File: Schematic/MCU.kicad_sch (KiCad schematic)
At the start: 23 parts, among them IC3 STM32H743VIT6, J1 USB_C_Receptacle_USB2.0_16P, SW1 TS24CA, Y1 Crystal

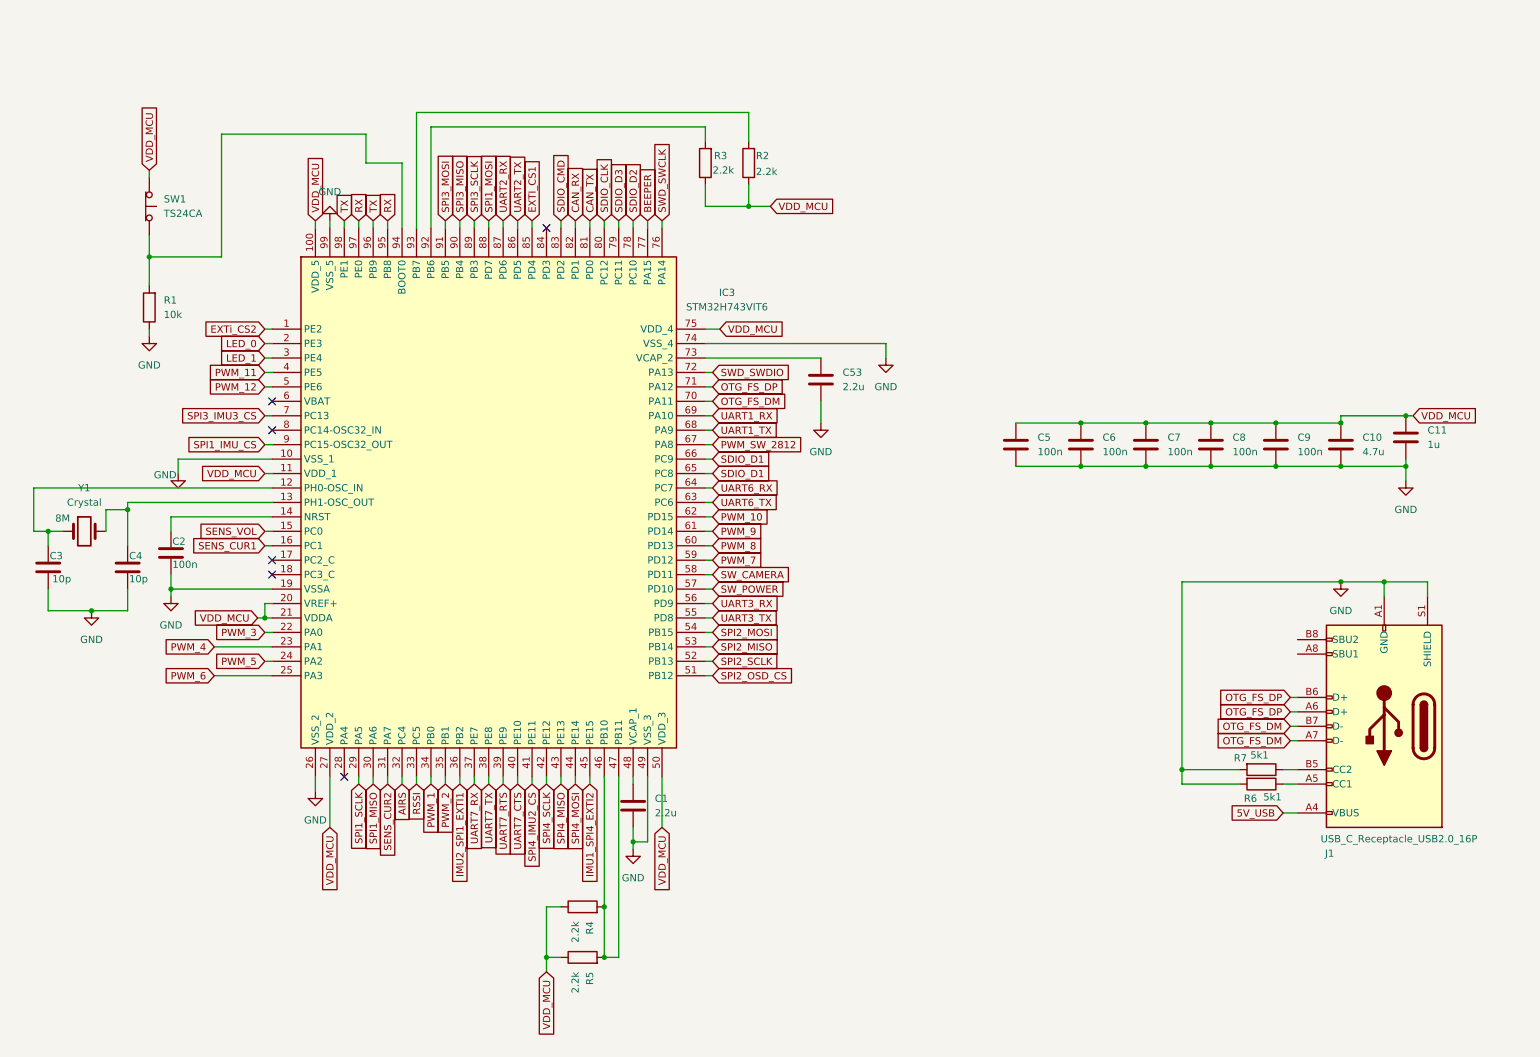
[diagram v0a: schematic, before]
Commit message: schematic fully finished, every footprint assigned, still electrical checking to do
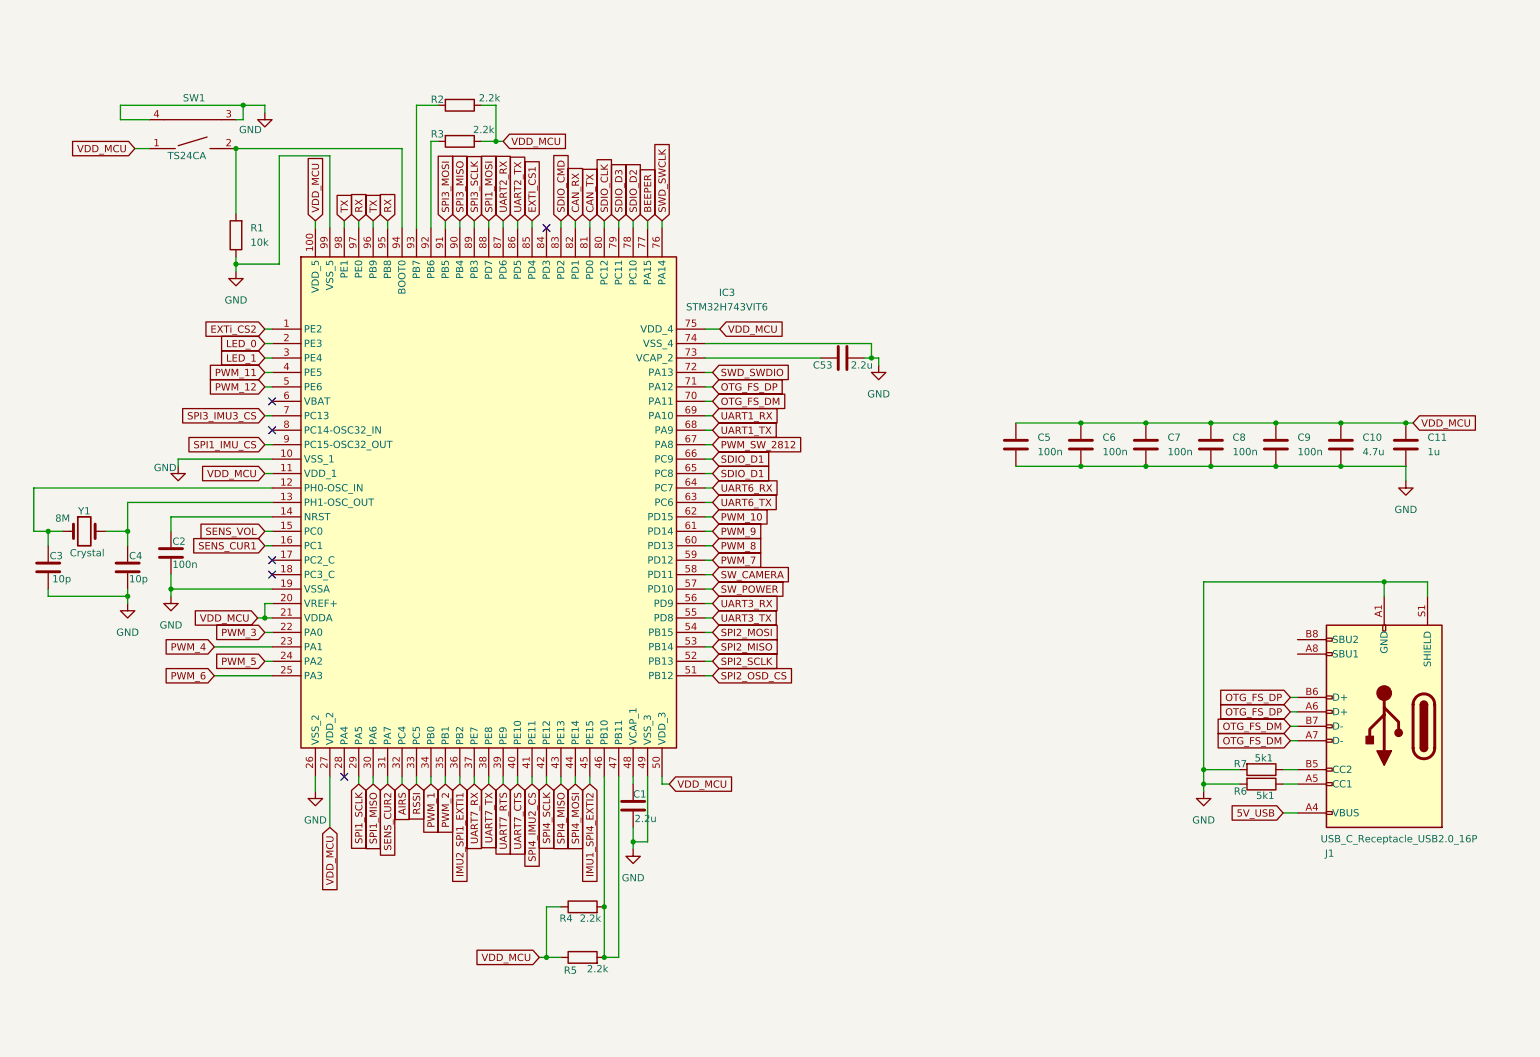
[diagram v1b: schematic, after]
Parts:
- removed SW1: TS24CA, symbol Switch:SW_Push_Open
- added SW1: TS24CA, ProLib_pcs_2025-11-24:SW-SMD_2P-TS24CA, symbol fch7_sym:TS24CA
- IC3: footprint QFP50P1600X1600X160-100M -> fch7_fp:QFP50P1600X1600X160-100M
- J1: MPN (none) -> USB4105-GF-A; ref USB4105-GF-A -> (none)
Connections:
- net GND: now also SW1.3, SW1.4
- net VDD_MCU: now also SW1.1
- net at IC3.94 (BOOT0), R1.2: now also SW1.2
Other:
- moved on the sheet: C11, C53, R1, R2, R3

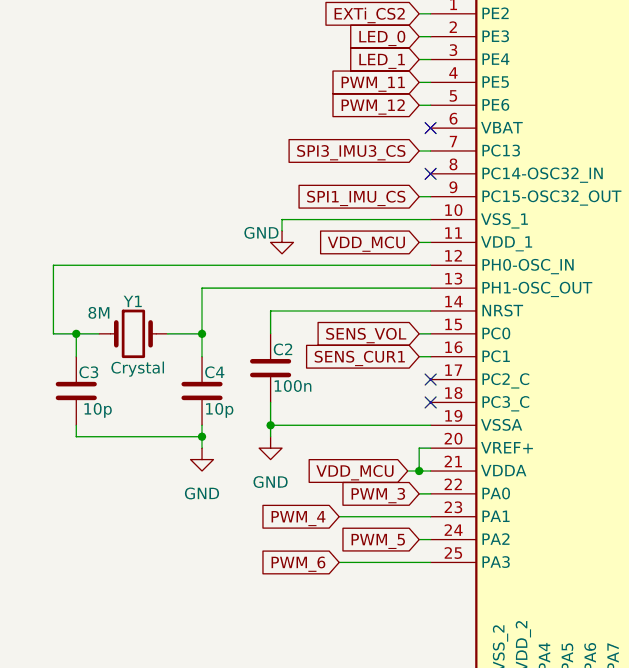
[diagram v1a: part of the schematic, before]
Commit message: reviewing and refactoring footprints and full schematic
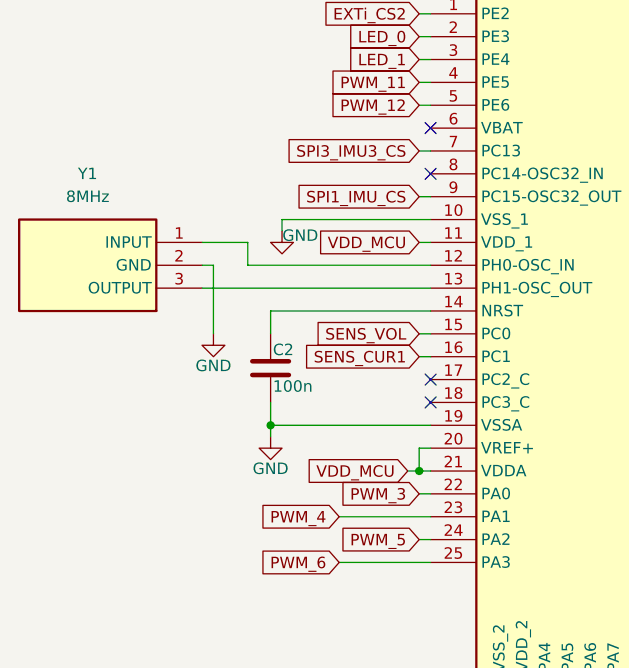
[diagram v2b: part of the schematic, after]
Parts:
- removed C3, C4: 10p, Capacitor_SMD:C_0603_1608Metric, symbol Device:C
- removed Y1: Crystal, Crystal:Crystal_SMD_3225-4Pin_3.2x2.5mm, symbol Device:Crystal
- added Y1: 8MHz, fch7_fp:CSTNE8M00G55Z000R0, symbol CSTNE8M00G55Z000R0:CSTNE8M00G55Z000R0
- C1, C53: footprint Capacitor_SMD:C_0805_2012Metric -> Capacitor_SMD:C_0603_1608Metric; MPN (none) -> CL10A225KB8NNNC; Manufacturer (none) -> SAMSUNG; Price (none) -> 0.095
- C10: footprint Capacitor_SMD:C_0805_2012Metric -> Capacitor_SMD:C_0603_1608Metric; MPN (none) -> CL10B105KO8NNNC; Manufacturer (none) -> SAMSUNG
- C11: MPN (none) -> CL10A105KB8NNNC; Manufacturer (none) -> SAMSUNG
- C2, C5, C6, C7, C8, C9: MPN (none) -> 0603B104K500NT; Manufacturer (none) -> FH
- IC3: MPN (none) -> STM32H743VIT6; Manufacturer (none) -> STM
- J1: footprint Connector_USB:USB_C_Receptacle_GCT_USB4105-xx-A_16P_TopMnt_Horizontal -> fch7_fp:USB-C-SMD_TYPE-C-6PIN-2MD-073; MPN USB4105-GF-A -> TYPE-C 16PIN 2MD(073); Manufacturer (none) -> SHOU HAN
- R1: MPN (none) -> 0603WAF1002T5E; Manufacturer (none) -> UNI-ROYAL
- R2, R3, R4, R5: MPN (none) -> 0603WAF2201T5E; Manufacturer (none) -> UNI-ROYAL
- R6, R7: MPN (none) -> 0603WAF5101T5E; Manufacturer (none) -> UNI-ROYAL
- SW1: MPN (none) -> TS24CA
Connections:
- net GND: now also Y1.2 (GND)
- net at IC3.12 (PH0-OSC_IN): now also Y1.1 (INPUT)
- net at IC3.13 (PH1-OSC_OUT): now also Y1.3 (OUTPUT)

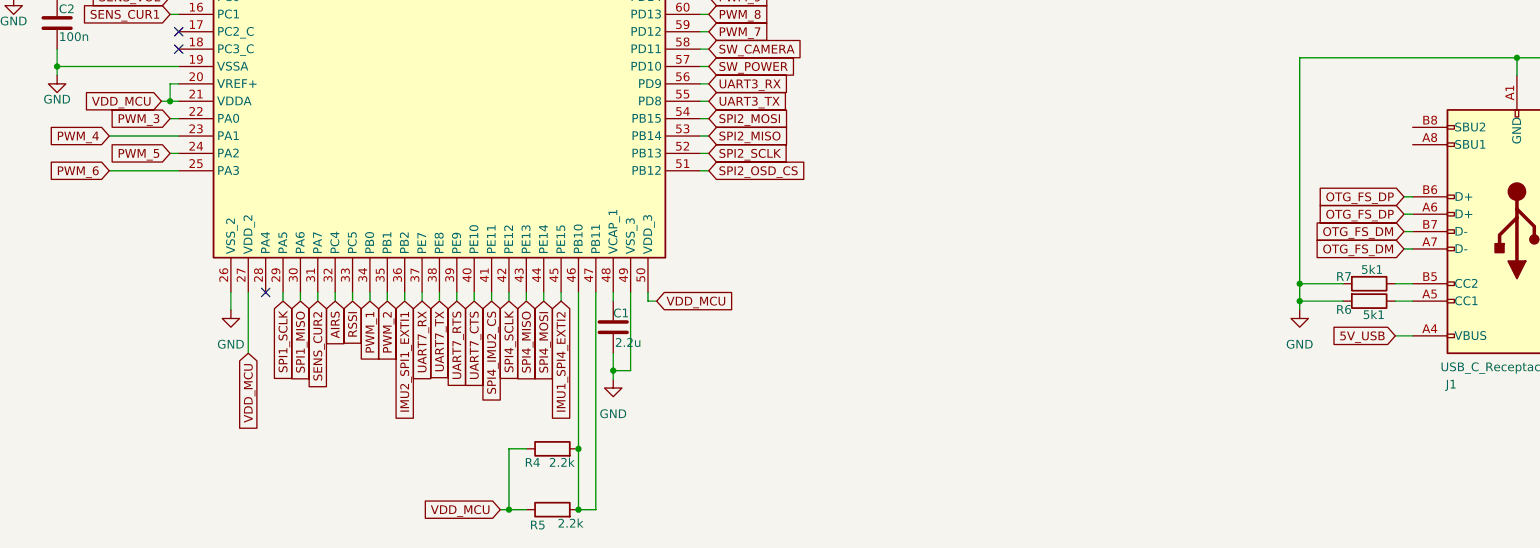
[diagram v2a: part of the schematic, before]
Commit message: Update schematic and footprint libraries with various component modifications
- Updated fp-info-cache with new component details and footprint changes.
- Modified osd.kicad_sch to correct pin types and add no_connect entries.
- Adjusted rf_rx.kicad_sch to fix pin assignments and update component properties.
- Enhanced sensors.kicad_sch with new properties for QMC5883L and SPL06-001 sensors.
- Added new libraries to sym-lib-table and fp-lib-table for better organization and access to components.
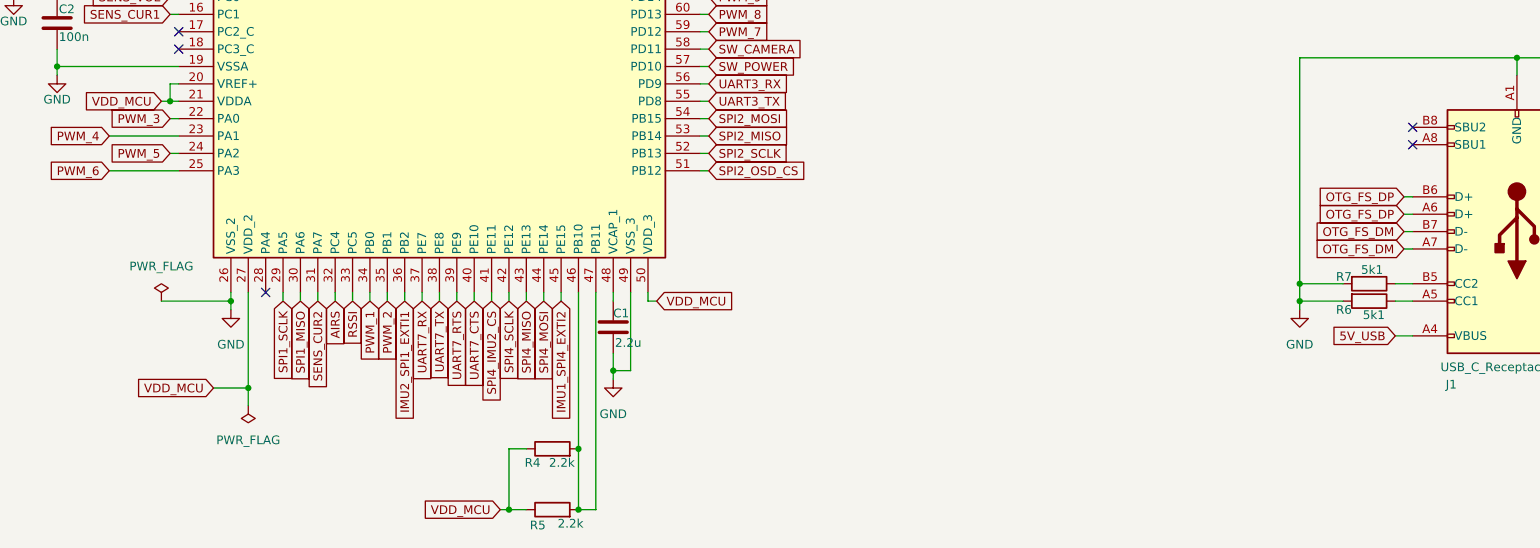
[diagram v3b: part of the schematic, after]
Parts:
- IC3: footprint fch7_fp:QFP50P1600X1600X160-100M -> fch7_fp:LQFP-100_14x14mm_P0.5mm_STM32H743
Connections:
- no-connect marks 6 -> 8
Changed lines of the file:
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@@
 	(paper "A4")
 	(junction
+		(at 71.12 148.59)
+		(diameter 0)
+		(color 0 0 0 0)
+	)
+	(junction
 		(at 205.74 85.09)
 		(diameter 0)
@@
 	)
 	(junction
+		(at 73.66 161.29)
+		(diameter 0)
+		(color 0 0 0 0)
+	)
+	(junction
 		(at 121.92 179.07)
 		(diameter 0)
@@
 	)
 	(no_connect
+		(at 243.84 123.19)
+	)
+	(no_connect
 		(at 63.5 111.76)
 	)
 	(no_connect
+		(at 243.84 125.73)
+	)
+	(no_connect
 		(at 76.2 147.32)
 	)
@@
 	(wire
 		(pts
-			(xy 73.66 147.32) (xy 73.66 156.21)
-		)
-		(stroke
-			(width 0)
-			(type default)
-		)
-	)
-	(wire
-		(pts
 			(xy 46.99 91.44) (xy 63.5 91.44)
 		)
@@
 	(wire
 		(pts
+			(xy 71.12 148.59) (xy 71.12 149.86)
+		)
+		(stroke
+			(width 0)
+			(type default)
+		)
+	)
+	(wire
+		(pts
 			(xy 58.42 31.75) (xy 58.42 29.21)
 		)
@@
 	(wire
 		(pts
+			(xy 73.66 161.29) (xy 73.66 163.83)
+		)
+		(stroke
+			(width 0)
+			(type default)
+		)
+	)
+	(wire
+		(pts
 			(xy 64.77 57.15) (xy 57.15 57.15)
 		)
@@
 	(wire
 		(pts
+			(xy 60.96 148.59) (xy 71.12 148.59)
+		)
+		(stroke
+			(width 0)
+			(type default)
+		)
+	)
+	(wire
+		(pts
 			(xy 241.3 153.67) (xy 243.84 153.67)
 		)
@@
 	(wire
 		(pts
+			(xy 68.58 161.29) (xy 73.66 161.29)
+		)
+		(stroke
+			(width 0)
+			(type default)
+		)
+	)
+	(wire
+		(pts
 			(xy 91.44 147.32) (xy 91.44 148.59)
 		)
@@
 	(wire
 		(pts
-			(xy 71.12 147.32) (xy 71.12 149.86)
-		)
-		(stroke
-			(width 0)
-			(type default)
-		)
-	)
-	(wire
-		(pts
 			(xy 57.15 55.88) (xy 57.15 57.15)
 		)
@@
 	(wire
 		(pts
+			(xy 73.66 147.32) (xy 73.66 161.29)
+		)
+		(stroke
+			(width 0)
+			(type default)
+		)
+	)
+	(wire
+		(pts
 			(xy 139.7 91.44) (xy 140.97 91.44)
 		)
@@
 	(wire
 		(pts
+			(xy 71.12 147.32) (xy 71.12 148.59)
+		)
+		(stroke
+			(width 0)
+			(type default)
+		)
+	)
+	(wire
+		(pts
 			(xy 132.08 148.59) (xy 133.35 148.59)
 		)
@@
 	(global_label "VDD_MCU"
 		(shape input)
-		(at 73.66 156.21 270)
+		(at 68.58 161.29 180)
 		(fields_autoplaced yes)
 		(effects
@@
 		)
 		(property "Intersheetrefs" "${INTERSHEET_REFS}"
-			(at 73.66 167.8433 90)
+			(at 56.9467 161.29 0)
 			(effects
 				(font
@@
 	)
 	(symbol
+		(lib_id "power:PWR_FLAG")
+		(at 73.66 163.83 180)
+		(unit 1)
+		(exclude_from_sim no)
+		(in_bom yes)
+		(on_board yes)
+		(dnp no)
+		(fields_autoplaced yes)
+		(property "Reference" "#FLG02"
+			(at 73.66 165.735 0)
+			(effects
+				(font
+					(size 1.27 1.27)
+				)
+				(hide yes)
+			)
+		)
+		(property "Value" "PWR_FLAG"
+			(at 73.66 168.91 0)
+			(effects
+				(font
+					(size 1.27 1.27)
+				)
+			)
+		)
+		(property "Footprint" ""
+			(at 73.66 163.83 0)
+			(effects
+				(font
+					(size 1.27 1.27)
+				)
+				(hide yes)
+			)
+		)
+		(property "Datasheet" "~"
+			(at 73.66 163.83 0)
+			(effects
+				(font
+					(size 1.27 1.27)
+				)
+				(hide yes)
+			)
+		)
+		(property "Description" "Special symbol for telling ERC where power comes from"
+			(at 73.66 163.83 0)
+			(effects
+				(font
+					(size 1.27 1.27)
+				)
+				(hide yes)
+			)
+		)
+		(pin "1"
+		)
+		(instances
+			(project "fch7"
+				(path "/11716af6-0e6e-444b-b738-3f12da23c1a2/0293db95-115d-42d2-990d-f9f4568d02e9"
+					(reference "#FLG02")
+					(unit 1)
+				)
+			)
+		)
+	)
+	(symbol
 		(lib_id "Device:R")
 		(at 237.49 148.59 270)
@@
 			)
 		)
-		(property "Footprint" "fch7_fp:QFP50P1600X1600X160-100M"
+		(property "Footprint" "fch7_fp:LQFP-100_14x14mm_P0.5mm_STM32H743"
 			(at 135.89 153.34 0)
 			(effects
@@
 					(unit 1)
 				)
+			)
+		)
+	)
+	(symbol
+		(lib_id "power:PWR_FLAG")
+		(at 60.96 148.59 0)
+		(unit 1)
+		(exclude_from_sim no)
+		(in_bom yes)
+		(on_board yes)
+		(dnp no)
+		(fields_autoplaced yes)
+		(property "Reference" "#FLG01"
+			(at 60.96 146.685 0)
+			(effects
+				(font
+					(size 1.27 1.27)
+				)
+				(hide yes)
+			)
+		)
+		(property "Value" "PWR_FLAG"
+			(at 60.96 143.51 0)
+			(effects
+				(font
+					(size 1.27 1.27)
+				)
+			)
+		)
+		(property "Footprint" ""
+			(at 60.96 148.59 0)
+			(effects
+				(font
+					(size 1.27 1.27)
+				)
+				(hide yes)
+			)
+		)
+		(property "Datasheet" "~"
+			(at 60.96 148.59 0)
+			(effects
+				(font
+					(size 1.27 1.27)
+				)
+				(hide yes)
+			)
+		)
+		(property "Description" "Special symbol for telling ERC where power comes from"
+			(at 60.96 148.59 0)
+			(effects
+				(font
+					(size 1.27 1.27)
+				)
+				(hide yes)
+			)
+		)
+		(pin "1"
+		)
+		(instances
+			(project ""
+				(path "/11716af6-0e6e-444b-b738-3f12da23c1a2/0293db95-115d-42d2-990d-f9f4568d02e9"
+					(reference "#FLG01")
+					(unit 1)
+				)
